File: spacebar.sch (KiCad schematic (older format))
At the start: 0 parts

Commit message: More work
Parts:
- added MX? (x2): MX-6U, symbol MX-6U
- added MX?: MX-6.25U, symbol MX-6.25U
- added MX?: MX-7U, symbol MX-7U
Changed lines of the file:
@@
 $Descr A4 11693 8268
 encoding utf-8
-Sheet 1 6
+Sheet 6 7
 Title ""
 Date ""
@@
 Comment4 ""
 $EndDescr
+$Comp
+L MX-6U MX?
+U 1 1 591DA43B
+P 3825 3400
+F 0 "MX?" H 3825 3525 60  0000 C CNN
+F 1 "MX-6U" H 3825 3450 20  0000 C CNN
+F 2 "" H 3800 3375 60  0001 C CNN
+F 3 "" H 3800 3375 60  0001 C CNN
+	1    3825 3400
+	1    0    0    -1
+$EndComp
+$Comp
+L MX-6U MX?
+U 1 1 591DA732
+P 4425 3400
+F 0 "MX?" H 4425 3525 60  0000 C CNN
+F 1 "MX-6U" H 4425 3450 20  0000 C CNN
+F 2 "" H 4400 3375 60  0001 C CNN
+F 3 "" H 4400 3375 60  0001 C CNN
+	1    4425 3400
+	1    0    0    -1
+$EndComp
+$Comp
+L MX-6.25U MX?
+U 1 1 591DA967
+P 5025 3400
+F 0 "MX?" H 5025 3525 60  0000 C CNN
+F 1 "MX-6.25U" H 5025 3450 20  0000 C CNN
+F 2 "" H 5000 3375 60  0001 C CNN
+F 3 "" H 5000 3375 60  0001 C CNN
+	1    5025 3400
+	1    0    0    -1
+$EndComp
+$Comp
+L MX-7U MX?
+U 1 1 591DAAC8
+P 5625 3400
+F 0 "MX?" H 5625 3525 60  0000 C CNN
+F 1 "MX-7U" H 5625 3450 20  0000 C CNN
+F 2 "" H 5600 3375 60  0001 C CNN
+F 3 "" H 5600 3375 60  0001 C CNN
+	1    5625 3400
+	1    0    0    -1
+$EndComp
 $EndSCHEMATC

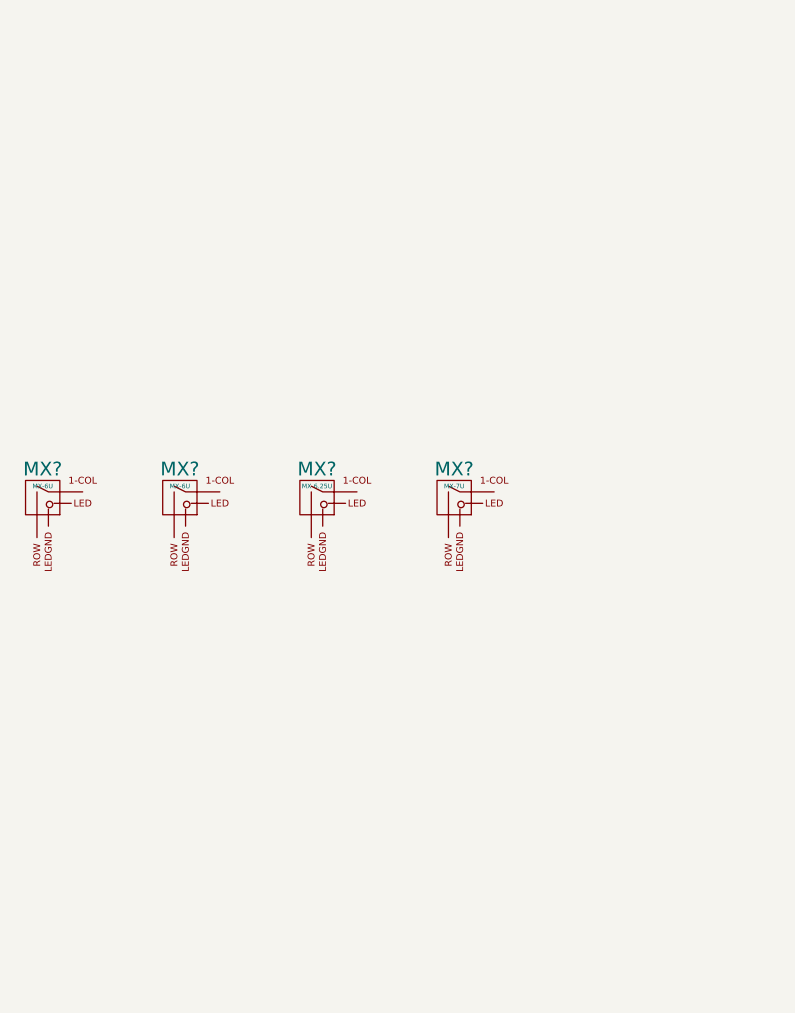
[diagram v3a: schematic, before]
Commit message: Added spacebar schematic
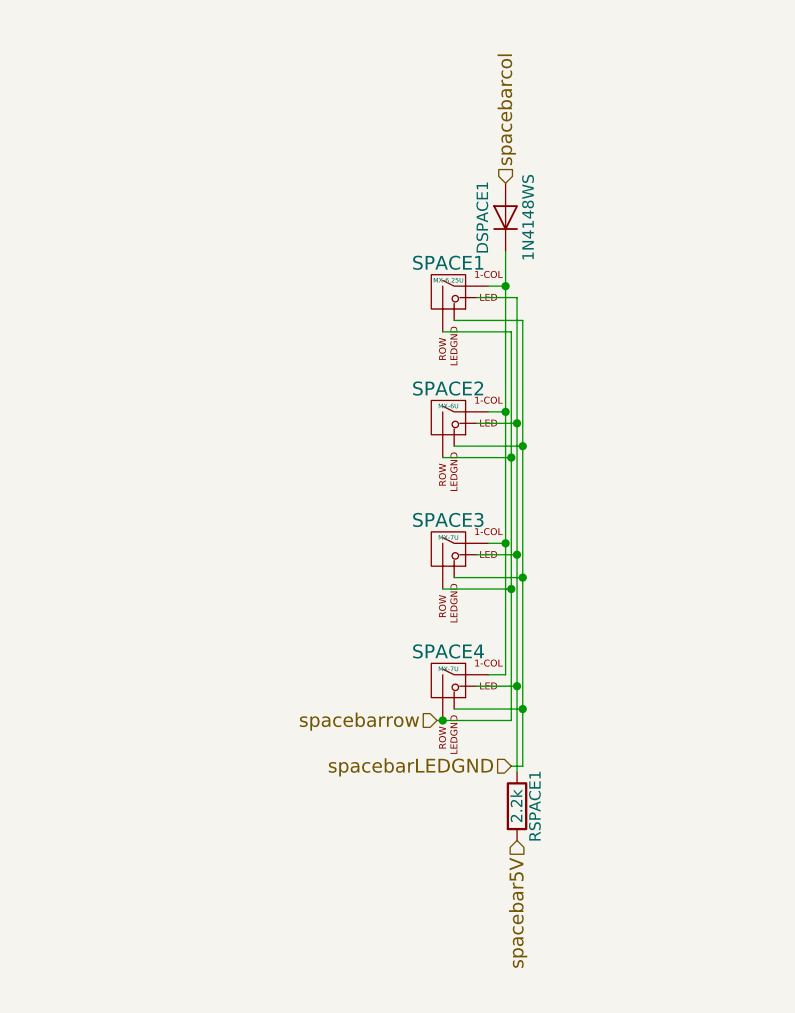
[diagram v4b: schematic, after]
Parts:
- removed MX? (x2): MX-6U, symbol MX-6U
- removed MX?: MX-6.25U, symbol MX-6.25U
- removed MX?: MX-7U, symbol MX-7U
- added DSPACE1: 1N4148WS, symbol D
- added RSPACE1: 2.2k, symbol R
- added SPACE1: MX-6.25U, symbol MX-6.25U
- added SPACE2: MX-6U, symbol MX-6U
- added SPACE3, SPACE4: MX-7U, symbol MX-7U
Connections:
- new net: DSPACE1.1 (K), SPACE1.1 (COL), SPACE2.1 (COL), SPACE3.1 (COL), SPACE4.1 (COL)
- new net: RSPACE1.1, SPACE1.3 (LED), SPACE2.3 (LED), SPACE3.3 (LED), SPACE4.3 (LED)
- new net spacebar5V: RSPACE1.2
- new net spacebarLEDGND: SPACE1.4 (LEDGND), SPACE2.4 (LEDGND), SPACE3.4 (LEDGND), SPACE4.4 (LEDGND)
- new net spacebarcol: DSPACE1.2 (A)
- new net spacebarrow: SPACE1.2 (ROW), SPACE2.2 (ROW), SPACE3.2 (ROW), SPACE4.2 (ROW)
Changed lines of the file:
@@
 LIBS:valves
 LIBS:MX_Alps_Hybrids
-LIBS:Matrix-cache
+LIBS:spacebar-cache
 EELAYER 25 0
 EELAYER END
 $Descr A4 11693 8268
 encoding utf-8
-Sheet 6 6
+Sheet 1 1
 Title ""
 Date ""
@@
 $EndDescr
 $Comp
-L MX-6U MX?
-U 1 1 591DA43B
-P 3825 3400
-F 0 "MX?" H 3825 3525 60  0000 C CNN
-F 1 "MX-6U" H 3825 3450 20  0000 C CNN
-F 2 "" H 3800 3375 60  0001 C CNN
-F 3 "" H 3800 3375 60  0001 C CNN
-	1    3825 3400
+L MX-6.25U SPACE1
+U 1 1 591D0149
+P 5600 2500
+F 0 "SPACE1" H 5600 2625 60  0000 C CNN
+F 1 "MX-6.25U" H 5600 2550 20  0000 C CNN
+F 2 "" H 5575 2475 60  0001 C CNN
+F 3 "" H 5575 2475 60  0001 C CNN
+	1    5600 2500
 	1    0    0    -1
 $EndComp
 $Comp
-L MX-6U MX?
-U 1 1 591DA732
-P 4425 3400
-F 0 "MX?" H 4425 3525 60  0000 C CNN
-F 1 "MX-6U" H 4425 3450 20  0000 C CNN
-F 2 "" H 4400 3375 60  0001 C CNN
-F 3 "" H 4400 3375 60  0001 C CNN
-	1    4425 3400
+L MX-6U SPACE2
+U 1 1 591D0192
+P 5600 3050
+F 0 "SPACE2" H 5600 3175 60  0000 C CNN
+F 1 "MX-6U" H 5600 3100 20  0000 C CNN
+F 2 "" H 5575 3025 60  0001 C CNN
+F 3 "" H 5575 3025 60  0001 C CNN
+	1    5600 3050
 	1    0    0    -1
 $EndComp
 $Comp
-L MX-6.25U MX?
-U 1 1 591DA967
-P 5025 3400
-F 0 "MX?" H 5025 3525 60  0000 C CNN
-F 1 "MX-6.25U" H 5025 3450 20  0000 C CNN
-F 2 "" H 5000 3375 60  0001 C CNN
-F 3 "" H 5000 3375 60  0001 C CNN
-	1    5025 3400
+L MX-7U SPACE3
+U 1 1 591D01E5
+P 5600 3625
+F 0 "SPACE3" H 5600 3750 60  0000 C CNN
+F 1 "MX-7U" H 5600 3675 20  0000 C CNN
+F 2 "" H 5575 3600 60  0001 C CNN
+F 3 "" H 5575 3600 60  0001 C CNN
+	1    5600 3625
 	1    0    0    -1
 $EndComp
 $Comp
-L MX-7U MX?
-U 1 1 591DAAC8
-P 5625 3400
-F 0 "MX?" H 5625 3525 60  0000 C CNN
-F 1 "MX-7U" H 5625 3450 20  0000 C CNN
-F 2 "" H 5600 3375 60  0001 C CNN
-F 3 "" H 5600 3375 60  0001 C CNN
-	1    5625 3400
+L MX-7U SPACE4
+U 1 1 591D023D
+P 5600 4200
+F 0 "SPACE4" H 5600 4325 60  0000 C CNN
+F 1 "MX-7U" H 5600 4250 20  0000 C CNN
+F 2 "" H 5575 4175 60  0001 C CNN
+F 3 "" H 5575 4175 60  0001 C CNN
+	1    5600 4200
 	1    0    0    -1
 $EndComp
+Wire Wire Line
+	5775 2475 5850 2475
+Wire Wire Line
+	5850 2325 5850 4175
+Wire Wire Line
+	5850 3025 5775 3025
+Wire Wire Line
+	5850 3600 5775 3600
+Connection ~ 5850 3025
+Wire Wire Line
+	5850 4175 5775 4175
+Connection ~ 5850 3600
+Wire Wire Line
+	5875 4375 5550 4375
+Wire Wire Line
+	5875 2675 5875 4375
+Wire Wire Line
+	5875 3800 5575 3800
+Wire Wire Line
+	5875 3225 5575 3225
+Connection ~ 5875 3800
+Wire Wire Line
+	5875 2675 5575 2675
+Connection ~ 5875 3225
+Wire Wire Line
+	5725 2525 5900 2525
+Wire Wire Line
+	5900 2525 5900 4600
+Wire Wire Line
+	5900 3075 5725 3075
+Wire Wire Line
+	5900 3650 5725 3650
+Connection ~ 5900 3075
+Wire Wire Line
+	5900 4225 5725 4225
+Connection ~ 5900 3650
+Wire Wire Line
+	5925 4325 5625 4325
+Wire Wire Line
+	5925 2625 5925 4575
+Wire Wire Line
+	5925 3750 5625 3750
+Wire Wire Line
+	5925 3175 5625 3175
+Connection ~ 5925 3750
+Wire Wire Line
+	5925 2625 5625 2625
+Connection ~ 5925 3175
+Text HLabel 5550 4375 0    60   Input ~ 0
+spacebarrow
+Connection ~ 5575 4375
+$Comp
+L D DSPACE1
+U 1 1 591D0C89
+P 5850 2175
+F 0 "DSPACE1" H 5850 2275 50  0000 C CNN
+F 1 "1N4148WS" H 5850 2075 50  0000 C CNN
+F 2 "" H 5850 2175 50  0000 C CNN
+F 3 "" H 5850 2175 50  0000 C CNN
+	1    5850 2175
+	0    -1   -1   0
+$EndComp
+Connection ~ 5850 2475
+Text HLabel 5850 2025 1    60   Input ~ 0
+spacebarcol
+Text HLabel 5900 4900 3    60   Input ~ 0
+spacebar5V
+Connection ~ 5900 4225
+Text HLabel 5875 4575 0    60   Input ~ 0
+spacebarLEDGND
+Connection ~ 5925 4325
+$Comp
+L R RSPACE1
+U 1 1 591D1231
+P 5900 4750
+F 0 "RSPACE1" V 5980 4750 50  0000 C CNN
+F 1 "2.2k" V 5900 4750 50  0000 C CNN
+F 2 "" V 5830 4750 50  0000 C CNN
+F 3 "" H 5900 4750 50  0000 C CNN
+	1    5900 4750
+	1    0    0    -1
+$EndComp
+Wire Wire Line
+	5925 4575 5875 4575
 $EndSCHEMATC

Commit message: Updated component labels
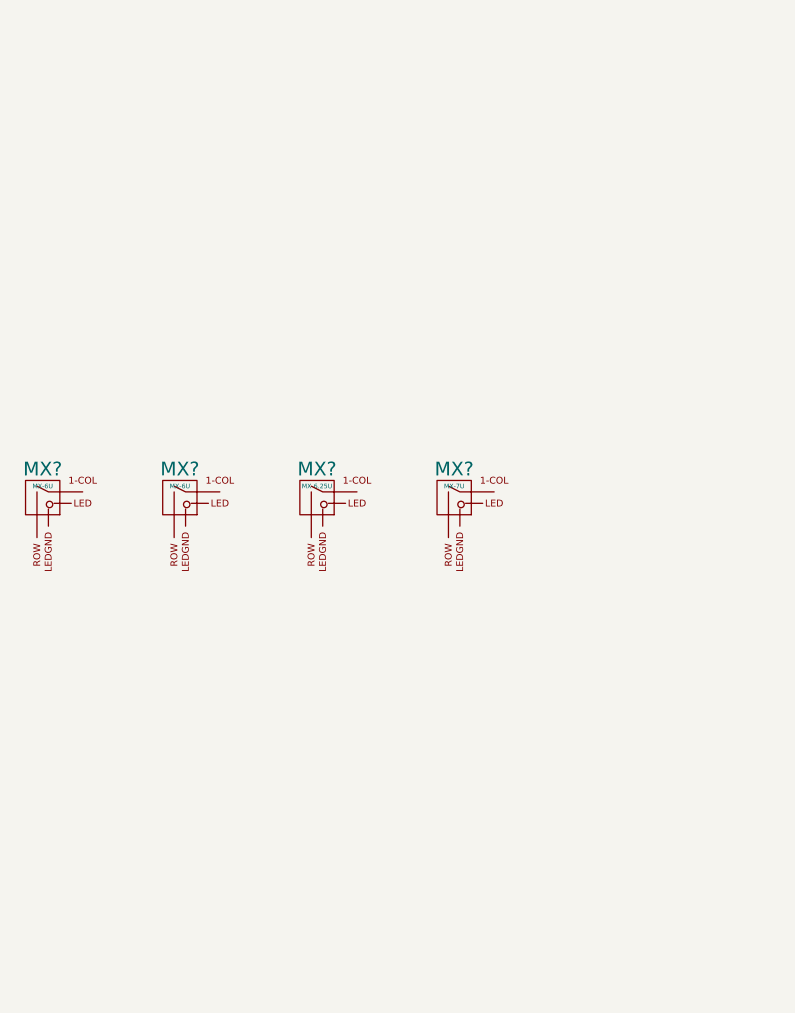
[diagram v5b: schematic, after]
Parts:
- removed DSPACE1: 1N4148WS, symbol D
- removed RSPACE1: 2.2k, symbol R
- removed SPACE1: MX-6.25U, symbol MX-6.25U
- removed SPACE2: MX-6U, symbol MX-6U
- removed SPACE3, SPACE4: MX-7U, symbol MX-7U
- added MX? (x2): MX-6U, symbol MX-6U
- added MX?: MX-6.25U, symbol MX-6.25U
- added MX?: MX-7U, symbol MX-7U
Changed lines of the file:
@@
 LIBS:valves
 LIBS:MX_Alps_Hybrids
-LIBS:spacebar-cache
+LIBS:Matrix-cache
 EELAYER 25 0
 EELAYER END
 $Descr A4 11693 8268
 encoding utf-8
-Sheet 1 1
+Sheet 6 6
 Title ""
 Date ""
@@
 $EndDescr
 $Comp
-L MX-6.25U SPACE1
-U 1 1 591D0149
-P 5600 2500
-F 0 "SPACE1" H 5600 2625 60  0000 C CNN
-F 1 "MX-6.25U" H 5600 2550 20  0000 C CNN
-F 2 "" H 5575 2475 60  0001 C CNN
-F 3 "" H 5575 2475 60  0001 C CNN
-	1    5600 2500
+L MX-6U MX?
+U 1 1 591DA43B
+P 3825 3400
+F 0 "MX?" H 3825 3525 60  0000 C CNN
+F 1 "MX-6U" H 3825 3450 20  0000 C CNN
+F 2 "" H 3800 3375 60  0001 C CNN
+F 3 "" H 3800 3375 60  0001 C CNN
+	1    3825 3400
 	1    0    0    -1
 $EndComp
 $Comp
-L MX-6U SPACE2
-U 1 1 591D0192
-P 5600 3050
-F 0 "SPACE2" H 5600 3175 60  0000 C CNN
-F 1 "MX-6U" H 5600 3100 20  0000 C CNN
-F 2 "" H 5575 3025 60  0001 C CNN
-F 3 "" H 5575 3025 60  0001 C CNN
-	1    5600 3050
+L MX-6U MX?
+U 1 1 591DA732
+P 4425 3400
+F 0 "MX?" H 4425 3525 60  0000 C CNN
+F 1 "MX-6U" H 4425 3450 20  0000 C CNN
+F 2 "" H 4400 3375 60  0001 C CNN
+F 3 "" H 4400 3375 60  0001 C CNN
+	1    4425 3400
 	1    0    0    -1
 $EndComp
 $Comp
-L MX-7U SPACE3
-U 1 1 591D01E5
-P 5600 3625
-F 0 "SPACE3" H 5600 3750 60  0000 C CNN
-F 1 "MX-7U" H 5600 3675 20  0000 C CNN
-F 2 "" H 5575 3600 60  0001 C CNN
-F 3 "" H 5575 3600 60  0001 C CNN
-	1    5600 3625
+L MX-6.25U MX?
+U 1 1 591DA967
+P 5025 3400
+F 0 "MX?" H 5025 3525 60  0000 C CNN
+F 1 "MX-6.25U" H 5025 3450 20  0000 C CNN
+F 2 "" H 5000 3375 60  0001 C CNN
+F 3 "" H 5000 3375 60  0001 C CNN
+	1    5025 3400
 	1    0    0    -1
 $EndComp
 $Comp
-L MX-7U SPACE4
-U 1 1 591D023D
-P 5600 4200
-F 0 "SPACE4" H 5600 4325 60  0000 C CNN
-F 1 "MX-7U" H 5600 4250 20  0000 C CNN
-F 2 "" H 5575 4175 60  0001 C CNN
-F 3 "" H 5575 4175 60  0001 C CNN
-	1    5600 4200
+L MX-7U MX?
+U 1 1 591DAAC8
+P 5625 3400
+F 0 "MX?" H 5625 3525 60  0000 C CNN
+F 1 "MX-7U" H 5625 3450 20  0000 C CNN
+F 2 "" H 5600 3375 60  0001 C CNN
+F 3 "" H 5600 3375 60  0001 C CNN
+	1    5625 3400
 	1    0    0    -1
 $EndComp
-Wire Wire Line
-	5775 2475 5850 2475
-Wire Wire Line
-	5850 2325 5850 4175
-Wire Wire Line
-	5850 3025 5775 3025
-Wire Wire Line
-	5850 3600 5775 3600
-Connection ~ 5850 3025
-Wire Wire Line
-	5850 4175 5775 4175
-Connection ~ 5850 3600
-Wire Wire Line
-	5875 4375 5550 4375
-Wire Wire Line
-	5875 2675 5875 4375
-Wire Wire Line
-	5875 3800 5575 3800
-Wire Wire Line
-	5875 3225 5575 3225
-Connection ~ 5875 3800
-Wire Wire Line
-	5875 2675 5575 2675
-Connection ~ 5875 3225
-Wire Wire Line
-	5725 2525 5900 2525
-Wire Wire Line
-	5900 2525 5900 4600
-Wire Wire Line
-	5900 3075 5725 3075
-Wire Wire Line
-	5900 3650 5725 3650
-Connection ~ 5900 3075
-Wire Wire Line
-	5900 4225 5725 4225
-Connection ~ 5900 3650
-Wire Wire Line
-	5925 4325 5625 4325
-Wire Wire Line
-	5925 2625 5925 4575
-Wire Wire Line
-	5925 3750 5625 3750
-Wire Wire Line
-	5925 3175 5625 3175
-Connection ~ 5925 3750
-Wire Wire Line
-	5925 2625 5625 2625
-Connection ~ 5925 3175
-Text HLabel 5550 4375 0    60   Input ~ 0
-spacebarrow
-Connection ~ 5575 4375
-$Comp
-L D DSPACE1
-U 1 1 591D0C89
-P 5850 2175
-F 0 "DSPACE1" H 5850 2275 50  0000 C CNN
-F 1 "1N4148WS" H 5850 2075 50  0000 C CNN
-F 2 "" H 5850 2175 50  0000 C CNN
-F 3 "" H 5850 2175 50  0000 C CNN
-	1    5850 2175
-	0    -1   -1   0
-$EndComp
-Connection ~ 5850 2475
-Text HLabel 5850 2025 1    60   Input ~ 0
-spacebarcol
-Text HLabel 5900 4900 3    60   Input ~ 0
-spacebar5V
-Connection ~ 5900 4225
-Text HLabel 5875 4575 0    60   Input ~ 0
-spacebarLEDGND
-Connection ~ 5925 4325
-$Comp
-L R RSPACE1
-U 1 1 591D1231
-P 5900 4750
-F 0 "RSPACE1" V 5980 4750 50  0000 C CNN
-F 1 "2.2k" V 5900 4750 50  0000 C CNN
-F 2 "" V 5830 4750 50  0000 C CNN
-F 3 "" H 5900 4750 50  0000 C CNN
-	1    5900 4750
-	1    0    0    -1
-$EndComp
-Wire Wire Line
-	5925 4575 5875 4575
 $EndSCHEMATC

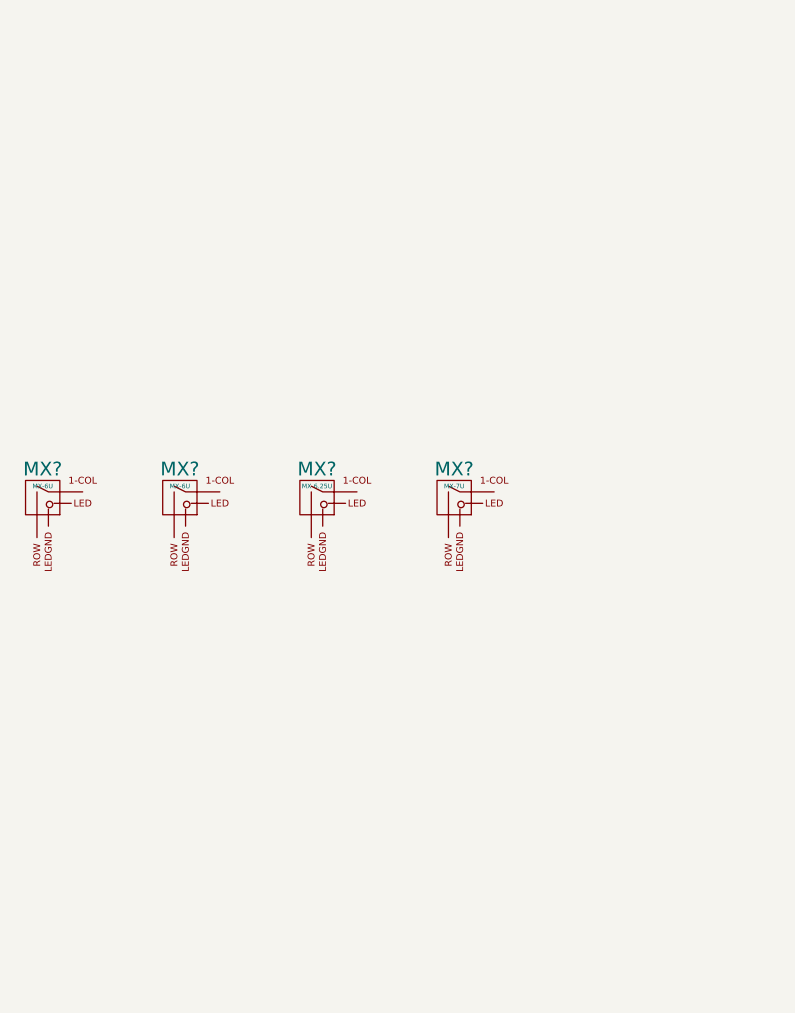
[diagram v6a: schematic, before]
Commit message: Finish Spacebar Routing
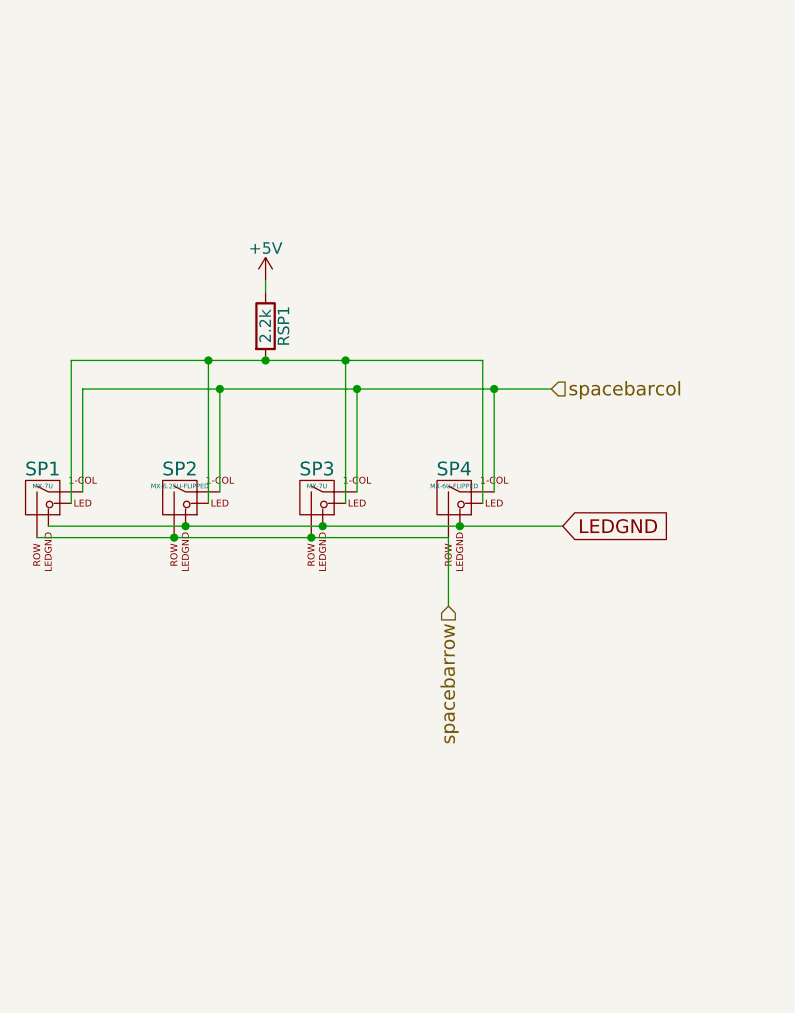
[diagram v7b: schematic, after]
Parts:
- removed MX? (x2): MX-6U, symbol MX-6U
- removed MX?: MX-6.25U, symbol MX-6.25U
- removed MX?: MX-7U, symbol MX-7U
- added RSP1: 2.2k, symbol R
- added SP1, SP3: MX-7U, symbol MX-7U
- added SP2: MX-6.25U-FLIPPED, symbol MX-6.25U-FLIPPED
- added SP4: MX-6U-FLIPPED, symbol MX-6U-FLIPPED
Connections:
- new net: RSP1.2, SP1.3 (LED), SP2.3 (LED), SP3.3 (LED), SP4.3 (LED)
- new net +5V: RSP1.1
- new net LEDGND: SP1.4 (LEDGND), SP2.4 (LEDGND), SP3.4 (LEDGND), SP4.4 (LEDGND)
- new net spacebarcol: SP1.1 (COL), SP2.2 (COL), SP3.1 (COL), SP4.2 (COL)
- new net spacebarrow: SP1.2 (ROW), SP2.1 (ROW), SP3.2 (ROW), SP4.1 (ROW)
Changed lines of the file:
@@
 $EndDescr
 $Comp
-L MX-6U MX?
-U 1 1 591DA43B
+L MX-7U SP1
+U 1 1 59353DBD
 P 3825 3400
-F 0 "MX?" H 3825 3525 60  0000 C CNN
-F 1 "MX-6U" H 3825 3450 20  0000 C CNN
+F 0 "SP1" H 3825 3525 60  0000 C CNN
+F 1 "MX-7U" H 3825 3450 20  0000 C CNN
 F 2 "" H 3800 3375 60  0001 C CNN
 F 3 "" H 3800 3375 60  0001 C CNN
@@
 $EndComp
 $Comp
-L MX-6U MX?
-U 1 1 591DA732
+L MX-7U SP3
+U 1 1 59353E7D
+P 5025 3400
+F 0 "SP3" H 5025 3525 60  0000 C CNN
+F 1 "MX-7U" H 5025 3450 20  0000 C CNN
+F 2 "" H 5000 3375 60  0001 C CNN
+F 3 "" H 5000 3375 60  0001 C CNN
+	1    5025 3400
+	1    0    0    -1
+$EndComp
+Wire Wire Line
+	3850 3525 6100 3525
+Connection ~ 5050 3525
+Text GLabel 6100 3525 2    60   Input ~ 0
+LEDGND
+$Comp
+L R RSP1
+U 1 1 593543DA
+P 4800 2650
+F 0 "RSP1" V 4880 2650 50  0000 C CNN
+F 1 "2.2k" V 4800 2650 50  0000 C CNN
+F 2 "" V 4730 2650 50  0001 C CNN
+F 3 "" H 4800 2650 50  0001 C CNN
+	1    4800 2650
+	1    0    0    -1
+$EndComp
+Wire Wire Line
+	3950 2800 5750 2800
+Wire Wire Line
+	3950 2800 3950 3425
+Wire Wire Line
+	4550 3425 4550 2800
+Connection ~ 4550 2800
+Wire Wire Line
+	5150 2800 5150 3425
+Connection ~ 4800 2800
+Wire Wire Line
+	5750 2800 5750 3425
+Connection ~ 5150 2800
+Wire Wire Line
+	4800 2500 4800 2450
+$Comp
+L +5V #PWR?
+U 1 1 59359514
+P 4800 2450
+F 0 "#PWR?" H 4800 2300 50  0001 C CNN
+F 1 "+5V" H 4800 2590 50  0000 C CNN
+F 2 "" H 4800 2450 50  0001 C CNN
+F 3 "" H 4800 2450 50  0001 C CNN
+	1    4800 2450
+	1    0    0    -1
+$EndComp
+$Comp
+L MX-6.25U-FLIPPED SP2
+U 1 1 593599DE
 P 4425 3400
-F 0 "MX?" H 4425 3525 60  0000 C CNN
-F 1 "MX-6U" H 4425 3450 20  0000 C CNN
+F 0 "SP2" H 4425 3525 60  0000 C CNN
+F 1 "MX-6.25U-FLIPPED" H 4425 3450 20  0000 C CNN
 F 2 "" H 4400 3375 60  0001 C CNN
 F 3 "" H 4400 3375 60  0001 C CNN
@@
 	1    0    0    -1
 $EndComp
+Connection ~ 4450 3525
 $Comp
-L MX-6.25U MX?
-U 1 1 591DA967
-P 5025 3400
-F 0 "MX?" H 5025 3525 60  0000 C CNN
-F 1 "MX-6.25U" H 5025 3450 20  0000 C CNN
-F 2 "" H 5000 3375 60  0001 C CNN
-F 3 "" H 5000 3375 60  0001 C CNN
-	1    5025 3400
-	1    0    0    -1
-$EndComp
-$Comp
-L MX-7U MX?
-U 1 1 591DAAC8
+L MX-6U-FLIPPED SP4
+U 1 1 59359F3B
 P 5625 3400
-F 0 "MX?" H 5625 3525 60  0000 C CNN
-F 1 "MX-7U" H 5625 3450 20  0000 C CNN
+F 0 "SP4" H 5625 3525 60  0000 C CNN
+F 1 "MX-6U-FLIPPED" H 5625 3450 20  0000 C CNN
 F 2 "" H 5600 3375 60  0001 C CNN
 F 3 "" H 5600 3375 60  0001 C CNN
@@
 	1    0    0    -1
 $EndComp
+Connection ~ 5650 3525
+Wire Wire Line
+	3800 3575 5600 3575
+Connection ~ 4400 3575
+Connection ~ 5000 3575
+Wire Wire Line
+	5600 3575 5600 3875
+Text HLabel 5600 3875 3    60   Input ~ 0
+spacebarrow
+Wire Wire Line
+	4000 3375 4000 2925
+Wire Wire Line
+	4000 2925 6050 2925
+Wire Wire Line
+	4600 2925 4600 3375
+Wire Wire Line
+	5200 2925 5200 3375
+Connection ~ 4600 2925
+Wire Wire Line
+	5800 2925 5800 3375
+Connection ~ 5200 2925
+Connection ~ 5800 2925
+Text HLabel 6050 2925 2    60   Input ~ 0
+spacebarcol
 $EndSCHEMATC

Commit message: Fixed spacebar
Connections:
- net +5V renamed spacebar5V
- net LEDGND renamed spacebarLEDGND
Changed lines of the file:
@@
 $Descr A4 11693 8268
 encoding utf-8
-Sheet 6 7
+Sheet 5 7
 Title ""
 Date ""
@@
 	3850 3525 6100 3525
 Connection ~ 5050 3525
-Text GLabel 6100 3525 2    60   Input ~ 0
-LEDGND
 $Comp
 L R RSP1
@@
 Wire Wire Line
 	4800 2500 4800 2450
-$Comp
-L +5V #PWR?
-U 1 1 59359514
-P 4800 2450
-F 0 "#PWR?" H 4800 2300 50  0001 C CNN
-F 1 "+5V" H 4800 2590 50  0000 C CNN
-F 2 "" H 4800 2450 50  0001 C CNN
-F 3 "" H 4800 2450 50  0001 C CNN
-	1    4800 2450
-	1    0    0    -1
-$EndComp
 $Comp
 L MX-6.25U-FLIPPED SP2
@@
 Text HLabel 6050 2925 2    60   Input ~ 0
 spacebarcol
+Text HLabel 6100 3525 2    60   Input ~ 0
+spacebarLEDGND
+Text HLabel 4800 2450 1    60   Input ~ 0
+spacebar5V
 $EndSCHEMATC
